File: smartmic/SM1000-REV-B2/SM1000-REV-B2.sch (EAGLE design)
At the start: 175 parts, among them CN1 HDR100-3, CN10 MJ-3523-SMT, CN11 HDR100-3, CN12 DF11-16DS, CN2 MOLEX-MINI-B-SMT, CN3 RASM712PX, CN4 RJ-45, CN5 MJ-3523-SMT, CN6 MJ-3523-SMT, CN7 MJ-3523-SMT, CN8 MJ-3523-SMT, CN9 MJ-3523-SMT, J1 JMP-2PIN, J2 JMP-2PIN, J3 JMP-2PIN, J4 JMP-2PIN, J5 JMP-2PIN, J7 JMP-2PIN, P1 TPAD50, P10 TPAD50, P11 TPAD50, P12 TPAD50, P13 TPAD50, P14 TPAD50, P15 TPAD50, P16 TPAD50, P17 TPAD50, P18 TPAD50, P19 TPAD50, P2 TPAD50, P20 TPAD50, P3 TPAD50, P4 TPAD50, P5 TPAD50, P6 TPAD50, P7 TPAD50, P8 TPAD50, P9 TPAD50, SW1 SW-BOURNS-7914S, SW2 SW-BOURNS-7914S, SW3 DPDT, SW4 SW-BOURNS-7914S, T1 SM-LP-5001, T2 SM-LP-5001, U1 STM32F405, U2 LD3985M33R, U3 STMPS2141, U4 EMIF02-USB03F2, U5 TPS54329E, U6 LMV341, U7 LMV341, U8 LM386M-1, U9 LMV341

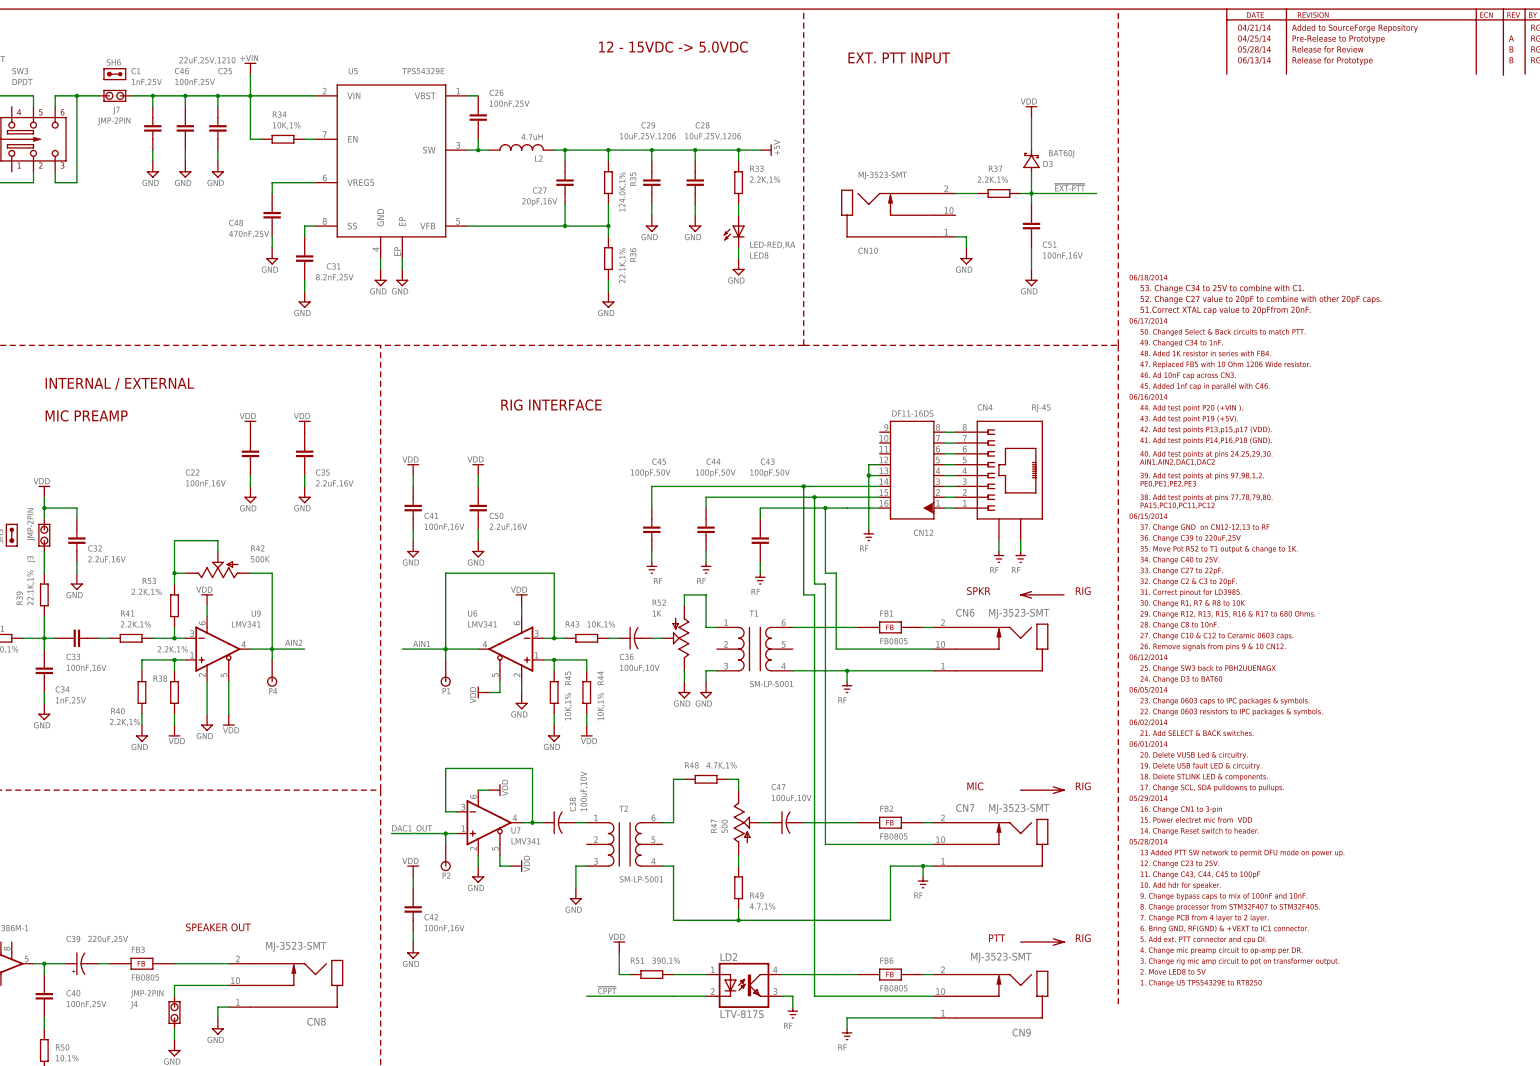
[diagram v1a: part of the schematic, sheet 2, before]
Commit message: 
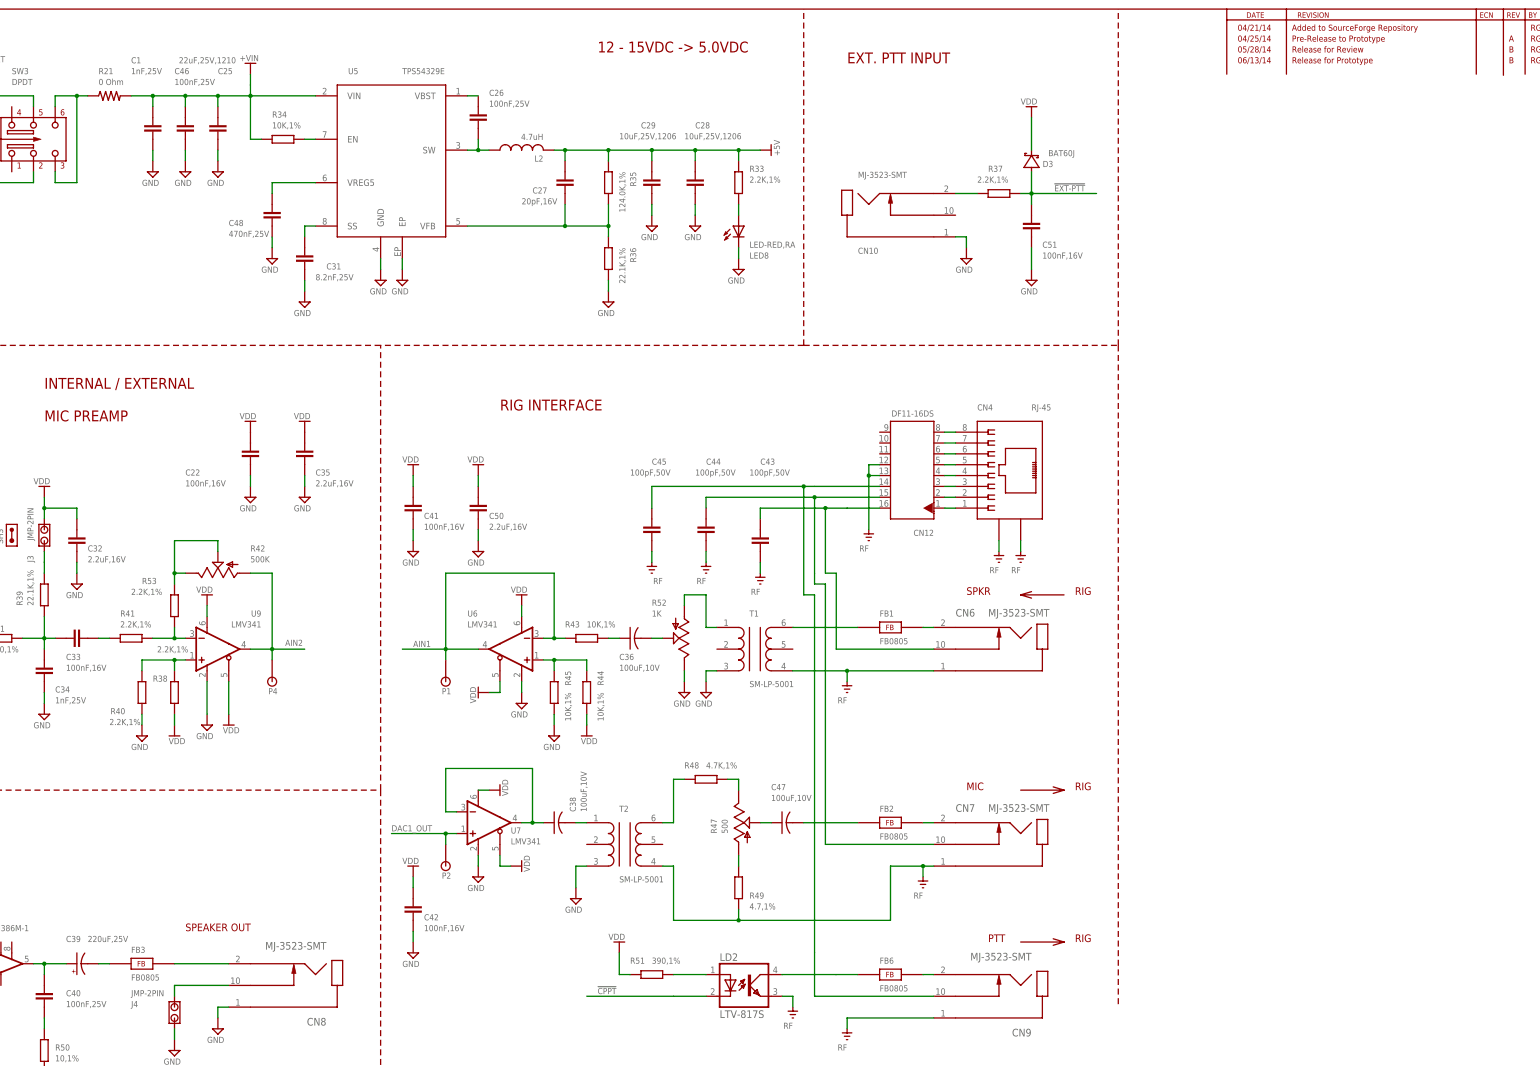
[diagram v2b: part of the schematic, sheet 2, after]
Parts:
- removed J2, J7: JMP-2PIN, _Coherix:JMP-2PIN
- removed SH2, SH6: SHUNT,0.1IN, _Coherix:SHUNT,0.1IN
- added R18, R21: 0 Ohm, _RoweTel:RES0805
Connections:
- net +3.3V: now also R18.1; no longer J2.1
- net +VIN: now also R21.2; no longer J7.1
- net N$70: now also R21.1; no longer J7.2
- net VDD: now also R18.2; no longer J2.2
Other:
- note removed: "05/28/2014"
- note removed: "05/29/2014"
- note removed: "06/01/2014"
- note removed: "06/02/2014"
- note removed: "06/05/2014"
- note removed: "06/12/2014"
- note removed: "06/15/2014"
- note removed: "06/16/2014"
- note removed: "06/17/2014"
- note removed: "06/18/2014"
- note removed: "1. Change U5 TPS54329E to RT8250"
- note removed: "10. Add hdr for speaker."
- note removed: "11. Change C43, C44, C45 to 100pF"
- note removed: "12. Change C23 to 25V."
- note removed: "13 Added PTT SW network to permit DFU mode on power up."
- note removed: "14. Change Reset switch to header."
- note removed: "15. Power electret mic from VDD"
- note removed: "16. Change CN1 to 3-pin"
- note removed: "17. Change SCL, SDA pulldowns to pullups."
- note removed: "18. Delete STLINK LED & components."
- note removed: "19. Delete USB fault LED & circuitry."
- note removed: "2. Move LED8 to 5V"
- note removed: "20. Delete VUSB Led & circuitry."
- note removed: "21. Add SELECT & BACK switches."
- note removed: "22. Change 0603 resistors to IPC packages & symbols."
- note removed: "23. Change 0603 caps to IPC packages & symbols."
- note removed: "24. Change D3 to BAT60"
- note removed: "25. Change SW3 back to PBH2UUENAGX"
- note removed: "26. Remove signals from pins 9 & 10 CN12."
- note removed: "27. Change C10 & C12 to Ceramic 0603 caps."
- note removed: "28. Change C8 to 10nF."
- note removed: "29. Change R12, R13, R15, R16 & R17 to 680 Ohms."
- note removed: "3. Change rig mic amp circuit to pot on transformer output."
- note removed: "30. Change R1, R7 & R8 to 10K"
- note removed: "31. Correct pinout for LD3985."
- note removed: "32. Change C2 & C3 to 20pF."
- note removed: "33. Change C27 to 22pF."
- note removed: "34. Change C40 to 25V."
- note removed: "35. Move Pot R52 to T1 output & change to 1K."
- note removed: "36. Change C39 to 220uF,25V"
- note removed: "37. Change GND on CN12-12,13 to RF"
- note removed: "38. Add test points at pins 77,78,79,80. PA15,PC10,PC11,PC12"
- note removed: "39. Add test points at pins 97,98,1,2. PE0,PE1,PE2,PE3"
- note removed: "4. Change mic preamp circuit to op-amp per DR."
- note removed: "40. Add test points at pins 24,25,29,30. AIN1,AIN2,DAC1,DAC2"
- note removed: "41. Add test points P14,P16,P18 (GND)."
- note removed: "42. Add test points P13,p15,p17 (VDD)."
- note removed: "43. Add test point P19 (+5V)."
- note removed: "44. Add test point P20 (+VIN )."
- note removed: "45. Added 1nf cap in parallel with C46."
- note removed: "46. Ad 10nF cap across CN3."
- note removed: "47. Replaced FB5 with 10 Ohm 1206 Wide resistor."
- note removed: "48. Aded 1K resistor in series with FB4."
- note removed: "49. Changed C34 to 1nF."
- note removed: "5. Add ext. PTT connector and cpu DI."
- note removed: "50. Changed Select & Back circuits to match PTT."
- note removed: "51.Correct XTAL cap value to 20pFfrom 20nF."
- note removed: "52. Change C27 value to 20pF to combine with other 20pF caps."
- note removed: "53. Change C34 to 25V to combine with C1."
- note removed: "6. Bring GND, RF(GND) & +VEXT to IC1 connector."
- note removed: "7. Change PCB from 4 layer to 2 layer."
- note removed: "8. Change processor from STM32F407 to STM32F405."
- note removed: "9. Change bypass caps to mix of 100nF and 10nF."

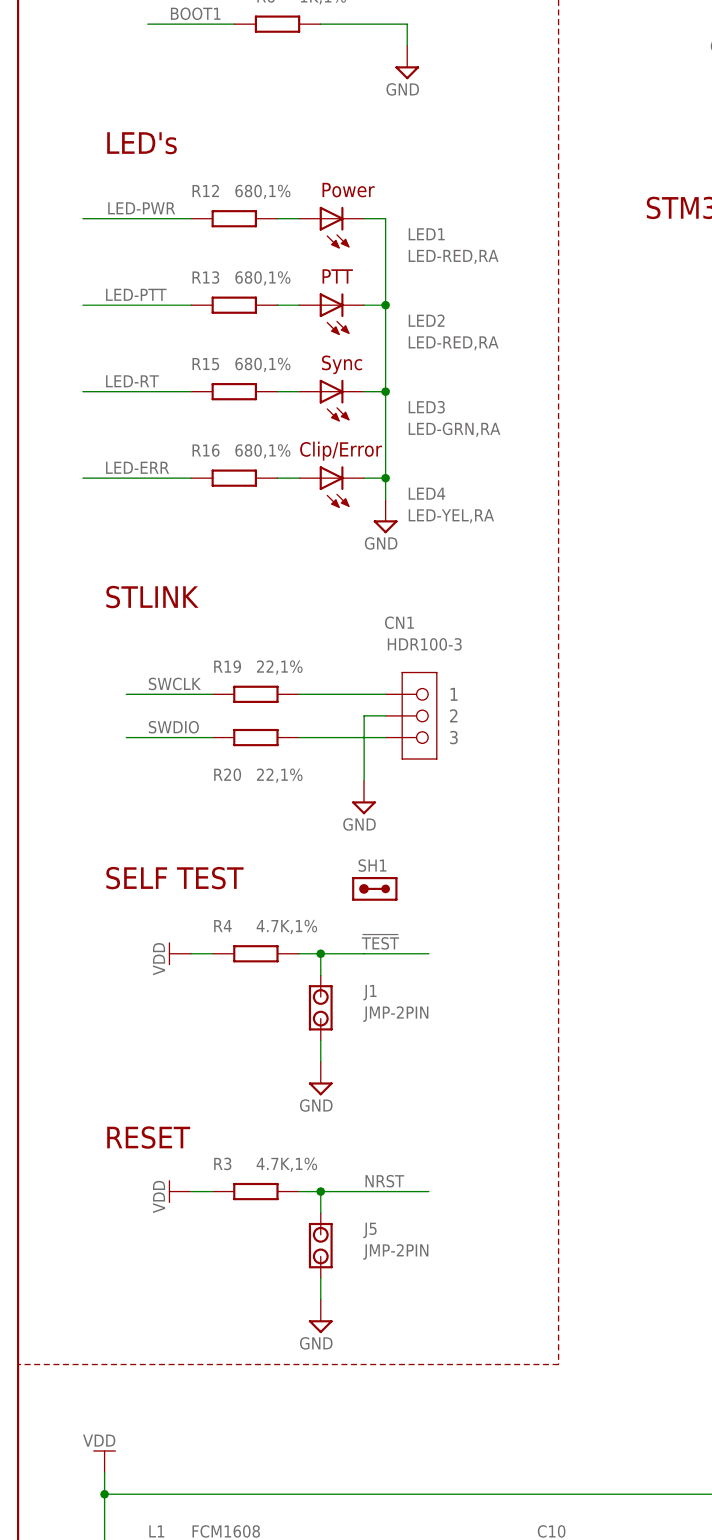
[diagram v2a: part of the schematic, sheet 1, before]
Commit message: Items 1-5,7-12,14-20 have been implemented in schematic . Items 6 & 13 need discussion to resolve. PCB has been updated to reflect changes, but routing of changes has not been completed. Layout will be updated as time pemits. RGB - 07/17/2014
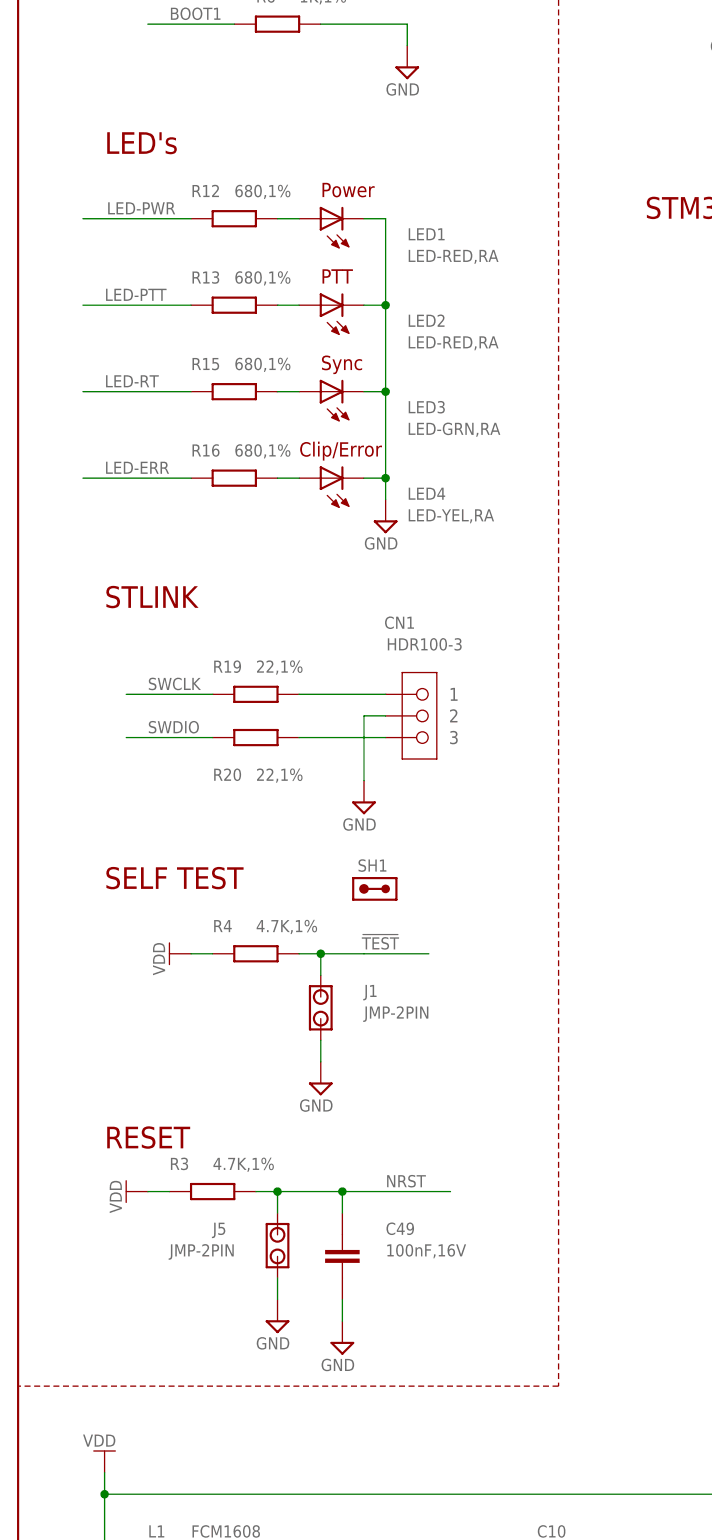
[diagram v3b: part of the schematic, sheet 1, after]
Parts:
- added C49: 100nF,16V, AA-ipc-7351-capacitor:CAPACITOR_0603
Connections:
- net GND: now also C49.2
- net NRST: now also C49.1
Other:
- moved on the sheet: J5, R3
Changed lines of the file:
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@@
 <part name="R18" library="_RoweTel" deviceset="RES0805" device="" value="0 Ohm"/>
 <part name="R21" library="_RoweTel" deviceset="RES0805" device="" value="0 Ohm"/>
+<part name="C49" library="AA-ipc-7351-capacitor" deviceset="CAPACITOR_" device="0603" value="100nF,16V"/>
+<part name="V124" library="A-SUPPLY2" deviceset="GND" device=""/>
 </parts>
 <sheets>
@@
 <plain>
 <wire x1="63.5" y1="279.4" x2="63.5" y2="228.6" width="0.1524" layer="94" style="longdash"/>
-<wire x1="63.5" y1="228.6" x2="63.5" y2="86.36" width="0.1524" layer="94" style="longdash"/>
-<wire x1="63.5" y1="86.36" x2="0" y2="86.36" width="0.1524" layer="94" style="longdash"/>
+<wire x1="63.5" y1="228.6" x2="63.5" y2="83.82" width="0.1524" layer="94" style="longdash"/>
+<wire x1="63.5" y1="83.82" x2="0" y2="83.82" width="0.1524" layer="94" style="longdash"/>
 <wire x1="185.42" y1="228.6" x2="185.42" y2="279.4" width="0.1524" layer="94" style="longdash"/>
 <wire x1="185.42" y1="228.6" x2="185.42" y2="210.82" width="0.1524" layer="94" style="longdash"/>
@@
 <instance part="V12" gate="G$1" x="17.78" y="259.08" rot="R90"/>
 <instance part="V13" gate="G$1" x="17.78" y="251.46" rot="R90"/>
-<instance part="J5" gate="G$1" x="35.56" y="99.06" smashed="yes" rot="R90">
-<attribute name="NAME" x="40.64" y="101.6" size="1.4224" layer="95"/>
-<attribute name="VALUE" x="40.64" y="99.06" size="1.4224" layer="96" ratio="9"/>
-</instance>
-<instance part="R3" gate="G$1" x="27.94" y="106.68" smashed="yes">
-<attribute name="NAME" x="22.86" y="109.22" size="1.4224" layer="95" ratio="9"/>
-<attribute name="VALUE" x="27.94" y="109.22" size="1.4224" layer="96" ratio="9"/>
-</instance>
-<instance part="V14" gate="GND" x="35.56" y="91.44"/>
-<instance part="V20" gate="G$1" x="20.32" y="106.68" rot="R90"/>
+<instance part="J5" gate="G$1" x="30.48" y="99.06" smashed="yes" rot="R90">
+<attribute name="NAME" x="22.86" y="101.6" size="1.4224" layer="95"/>
+<attribute name="VALUE" x="17.78" y="99.06" size="1.4224" layer="96" ratio="9"/>
+</instance>
+<instance part="R3" gate="G$1" x="22.86" y="106.68" smashed="yes">
+<attribute name="NAME" x="17.78" y="109.22" size="1.4224" layer="95" ratio="9"/>
+<attribute name="VALUE" x="22.86" y="109.22" size="1.4224" layer="96" ratio="9"/>
+</instance>
+<instance part="V14" gate="GND" x="30.48" y="91.44"/>
+<instance part="V20" gate="G$1" x="15.24" y="106.68" rot="R90"/>
 <instance part="SW2" gate="G$1" x="243.84" y="241.3" smashed="yes" rot="R90">
 <attribute name="NAME" x="248.92" y="251.46" size="1.4224" layer="95" ratio="10"/>
@@
 <instance part="U$3" gate="G$1" x="114.3" y="266.7"/>
 <instance part="R18" gate="G$1" x="297.18" y="154.94"/>
+<instance part="C49" gate="G$1" x="38.1" y="99.06" smashed="yes" rot="R270">
+<attribute name="NAME" x="43.18" y="101.6" size="1.4224" layer="95" ratio="9"/>
+<attribute name="VALUE" x="43.18" y="99.06" size="1.4224" layer="96" ratio="9"/>
+</instance>
+<instance part="V124" gate="GND" x="38.1" y="88.9"/>
 </instances>
 <busses>
@@
 <segment>
 <pinref part="R3" gate="G$1" pin="1"/>
-<wire x1="22.86" y1="106.68" x2="20.32" y2="106.68" width="0.1524" layer="91"/>
 <pinref part="V20" gate="G$1" pin="VDD"/>
+<wire x1="15.24" y1="106.68" x2="17.78" y2="106.68" width="0.1524" layer="91"/>
 </segment>
 <segment>
@@
 <segment>
 <pinref part="J5" gate="G$1" pin="1"/>
-<wire x1="35.56" y1="96.52" x2="35.56" y2="93.98" width="0.1524" layer="91"/>
+<wire x1="30.48" y1="96.52" x2="30.48" y2="93.98" width="0.1524" layer="91"/>
 <pinref part="V14" gate="GND" pin="GND"/>
 </segment>
@@
 <wire x1="281.94" y1="218.44" x2="281.94" y2="220.98" width="0.1524" layer="91"/>
 </segment>
+<segment>
+<pinref part="C49" gate="G$1" pin="2"/>
+<wire x1="38.1" y1="93.98" x2="38.1" y2="91.44" width="0.1524" layer="91"/>
+<pinref part="V124" gate="GND" pin="GND"/>
+</segment>
 </net>
 <net name="SCL" class="0">
@@
 <pinref part="R3" gate="G$1" pin="2"/>
 <pinref part="J5" gate="G$1" pin="2"/>
-<wire x1="33.02" y1="106.68" x2="35.56" y2="106.68" width="0.1524" layer="91"/>
-<wire x1="35.56" y1="106.68" x2="35.56" y2="104.14" width="0.1524" layer="91"/>
-<wire x1="35.56" y1="106.68" x2="48.26" y2="106.68" width="0.1524" layer="91"/>
-<junction x="35.56" y="106.68"/>
-<label x="40.64" y="107.188" size="1.4224" layer="95" ratio="10"/>
+<wire x1="27.94" y1="106.68" x2="30.48" y2="106.68" width="0.1524" layer="91"/>
+<wire x1="30.48" y1="106.68" x2="30.48" y2="104.14" width="0.1524" layer="91"/>
+<wire x1="30.48" y1="106.68" x2="38.1" y2="106.68" width="0.1524" layer="91"/>
+<junction x="30.48" y="106.68"/>
+<label x="43.18" y="107.188" size="1.4224" layer="95" ratio="10"/>
+<pinref part="C49" gate="G$1" pin="1"/>
+<wire x1="38.1" y1="106.68" x2="50.8" y2="106.68" width="0.1524" layer="91"/>
+<wire x1="38.1" y1="104.14" x2="38.1" y2="106.68" width="0.1524" layer="91"/>
+<junction x="38.1" y="106.68"/>
 </segment>
 </net>
